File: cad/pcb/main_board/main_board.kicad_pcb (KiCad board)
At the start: 2 copper layers, 69.8 x 55.5 mm, 76 parts, among them J1 USB_B_Micro, J2 Conn_ARM_JTAG_SWD_10, U1 STM32F401R_B-C_Tx, U2 TLV75533PDRVR, Y1 Crystal_GND23

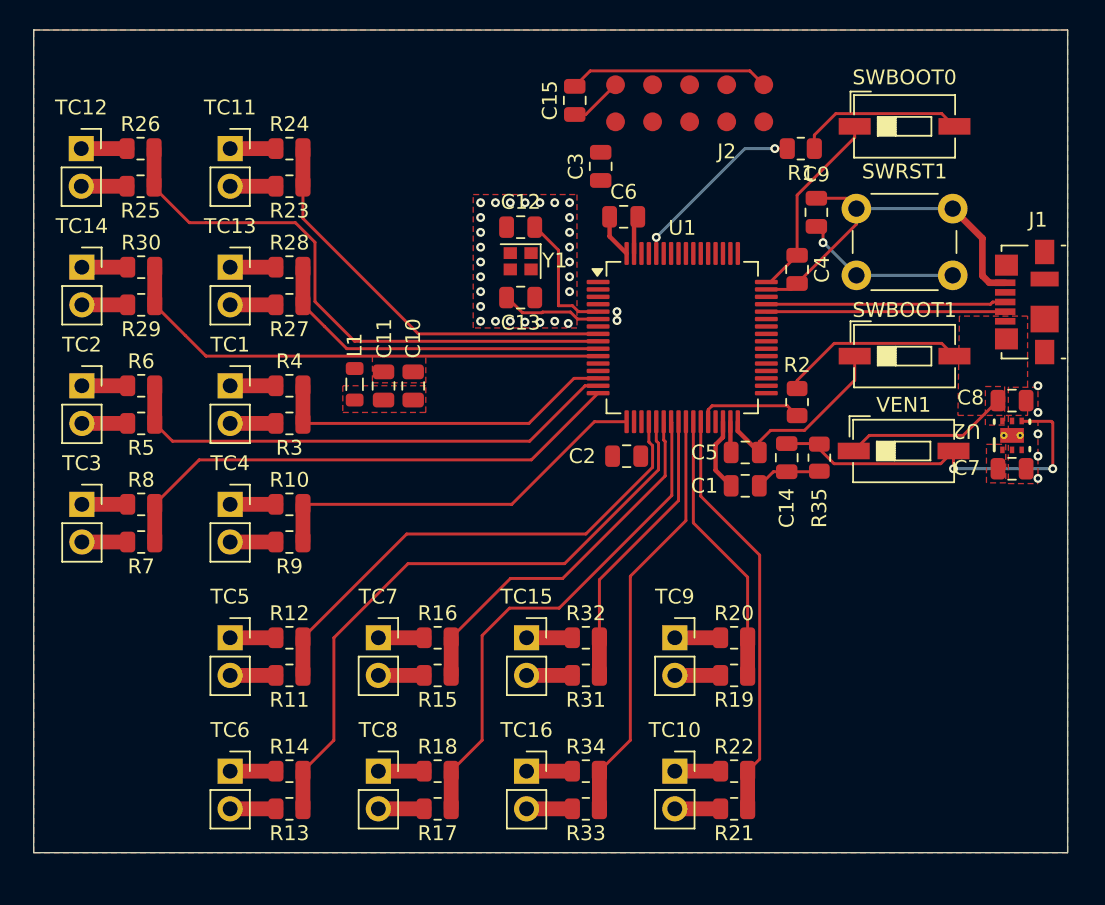
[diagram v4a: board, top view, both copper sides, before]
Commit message: Connecting NRST, placing VSS Vias next to MCU Pins
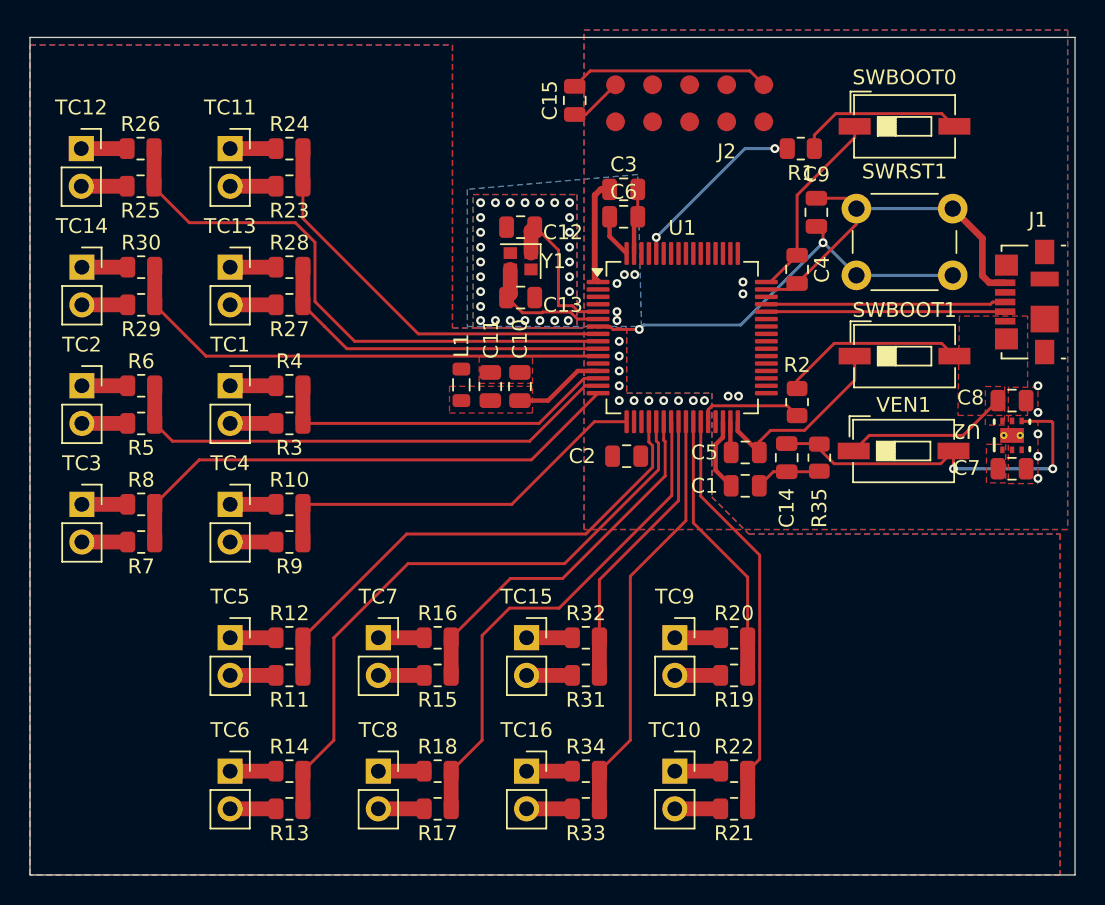
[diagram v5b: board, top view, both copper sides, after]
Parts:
- moved C10 7.20 mm to (98.5, 56.0)
- moved C11 7.20 mm to (96.5, 56.0)
- moved L1 7.20 mm to (94.6, 55.9)
- moved C3 2.19 mm to (105.5, 42.8), turned to 0 degrees
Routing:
- net Net-(U1-NRST): track 10.9 -> 28.6 mm, vias 1 -> 2
- net VDD: track 32.9 -> 40.0 mm
- net VDDA: track 0.00 -> 6.10 mm
- net Net-(U1-PH1): track 6.84 -> 8.84 mm
- net Net-(U1-PH0): track 9.21 -> 11.1 mm
- net VSS: track 35.5 -> 37.4 mm, vias 34 -> 41
- net VSSA: vias 0 -> 11
- added copper zone on B.Cu, net VSSA
- added copper zone on F.Cu, net VSSA
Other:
- board size 69.8 x 55.5 mm -> 70.5 x 56.5 mm

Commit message: Power SUpply Struggles
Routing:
- net VDD: track 40.0 -> 72.9 mm, vias 0 -> 1
- net Net-(R2-Pad1): track 12.6 -> 2.12 mm, vias 0 -> 1
- net VBUS: track 11.1 -> 1.48 mm
- net VSS: track 37.4 -> 40.3 mm
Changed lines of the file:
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@@
+	)
+	(segment
+		(start 106.25 59.30312)
+		(end 104.80312 60.75)
+		(width 0.3)
+		(layer "F.Cu")
+		(net 2)
+	)
+	(segment
+		(start 104.80312 60.75)
+		(end 104.8 60.75)
+		(width 0.3)
+		(layer "F.Cu")
+		(net 2)
+	)
+	(segment
+		(start 106.25 58.425)
+		(end 106.25 59.30312)
+		(width 0.3)
+		(layer "F.Cu")
+		(net 2)
 	)
 	(segment
@@
 	)
 	(segment
-		(start 117.75 59.009744)
-		(end 115.465256 59.009744)
-		(width 0.2)
-		(layer "F.Cu")
-		(net 3)
-	)
-	(segment
 		(start 104 42.75)
 		(end 104.6 42.75)
@@
 	)
 	(segment
+		(start 104.6 42.75)
+		(end 104.6 44.6)
+		(width 0.4)
+		(layer "F.Cu")
+		(net 3)
+	)
+	(segment
 		(start 117.25 47.2)
 		(end 115.45 49)
@@
 	)
 	(segment
+		(start 130.8 61.6)
+		(end 129.58 60.38)
+		(width 1)
+		(layer "F.Cu")
+		(net 3)
+	)
+	(segment
+		(start 106.75 58.425)
+		(end 106.75 60.7)
+		(width 0.3)
+		(layer "F.Cu")
+		(net 3)
+	)
+	(segment
+		(start 114.7 59.775)
+		(end 115.465256 59.009744)
+		(width 0.4)
+		(layer "F.Cu")
+		(net 3)
+	)
+	(segment
 		(start 103.6 43.15)
 		(end 104 42.75)
@@
 	)
 	(segment
+		(start 121.135 55.765)
+		(end 121.135 54)
+		(width 0.4)
+		(layer "F.Cu")
+		(net 3)
+	)
+	(segment
 		(start 121.135 38.5)
 		(end 121.135 39.255256)
@@
 	)
 	(segment
-		(start 121.135 55.624744)
-		(end 121.135 54)
-		(width 0.2)
+		(start 114.7 60.5)
+		(end 114.7 59.775)
+		(width 0.4)
 		(layer "F.Cu")
 		(net 3)
@@
 	)
 	(segment
-		(start 117.75 59.009744)
-		(end 121.135 55.624744)
-		(width 0.2)
+		(start 111.675 41.625)
+		(end 117.25 47.2)
+		(width 0.4)
 		(layer "F.Cu")
 		(net 3)
@@
 	)
 	(segment
+		(start 117.890256 59.009744)
+		(end 121.135 55.765)
+		(width 0.4)
+		(layer "F.Cu")
+		(net 3)
+	)
+	(segment
+		(start 105.725 41.625)
+		(end 111.675 41.625)
+		(width 0.4)
+		(layer "F.Cu")
+		(net 3)
+	)
+	(segment
+		(start 105.725 41.625)
+		(end 105.725 41.175)
+		(width 0.4)
+		(layer "F.Cu")
+		(net 3)
+	)
+	(segment
+		(start 104.6 42.75)
+		(end 105.725 41.625)
+		(width 0.4)
+		(layer "F.Cu")
+		(net 3)
+	)
+	(segment
 		(start 104.6 45.925)
 		(end 105.75 47.075)
@@
 	)
 	(segment
-		(start 115.465256 59.009744)
-		(end 114.7 59.775)
-		(width 0.2)
+		(start 129.58 60.38)
+		(end 129.58 59.3)
+		(width 1)
+		(layer "F.Cu")
+		(net 3)
+	)
+	(segment
+		(start 105.725 41.175)
+		(end 102.25 37.7)
+		(width 0.4)
+		(layer "F.Cu")
+		(net 3)
+	)
+	(segment
+		(start 129.58 59.3)
+		(end 126.045 55.765)
+		(width 1)
 		(layer "F.Cu")
 		(net 3)
@@
 	)
 	(segment
-		(start 114.7 59.775)
-		(end 114.7 60.5)
-		(width 0.2)
-		(layer "F.Cu")
-		(net 3)
-	)
-	(segment
-		(start 128.45 59.35)
-		(end 130.8 57)
-		(width 0.2)
-		(layer "F.Cu")
-		(net 4)
-	)
-	(segment
-		(start 122.12 59.35)
-		(end 128.45 59.35)
-		(width 0.2)
-		(layer "F.Cu")
-		(net 4)
+		(start 106.75 60.7)
+		(end 106.7 60.75)
+		(width 0.3)
+		(layer "F.Cu")
+		(net 3)
+	)
+	(segment
+		(start 115.465256 59.009744)
+		(end 117.890256 59.009744)
+		(width 0.4)
+		(layer "F.Cu")
+		(net 3)
+	)
+	(via
+		(at 126.045 55.765)
+		(size 0.6)
+		(drill 0.3)
+		(layers "F.Cu" "B.Cu")
+		(net 3)
 	)
 	(segment
@@
 	)
 	(segment
-		(start 117.25 55.645)
-		(end 119.755 53.14)
-		(width 0.2)
-		(layer "F.Cu")
-		(net 16)
-	)
-	(segment
 		(start 117.25 56.1875)
 		(end 117.25 55.645)
@@
 	)
 	(segment
-		(start 119.755 53.14)
-		(end 127.005 53.14)
+		(start 117.25 55.645)
+		(end 117.25 55.35)
+		(width 0.2)
+		(layer "F.Cu")
+		(net 16)
+	)
+	(segment
+		(start 117.25 55.35)
+		(end 117.2 55.3)
 		(width 0.2)
 		(layer "F.Cu")
@@
 		(net 16)
 	)
+	(via
+		(at 117.2 55.3)
+		(size 0.6)
+		(drill 0.3)
+		(layers "F.Cu" "B.Cu")
+		(net 16)
+	)

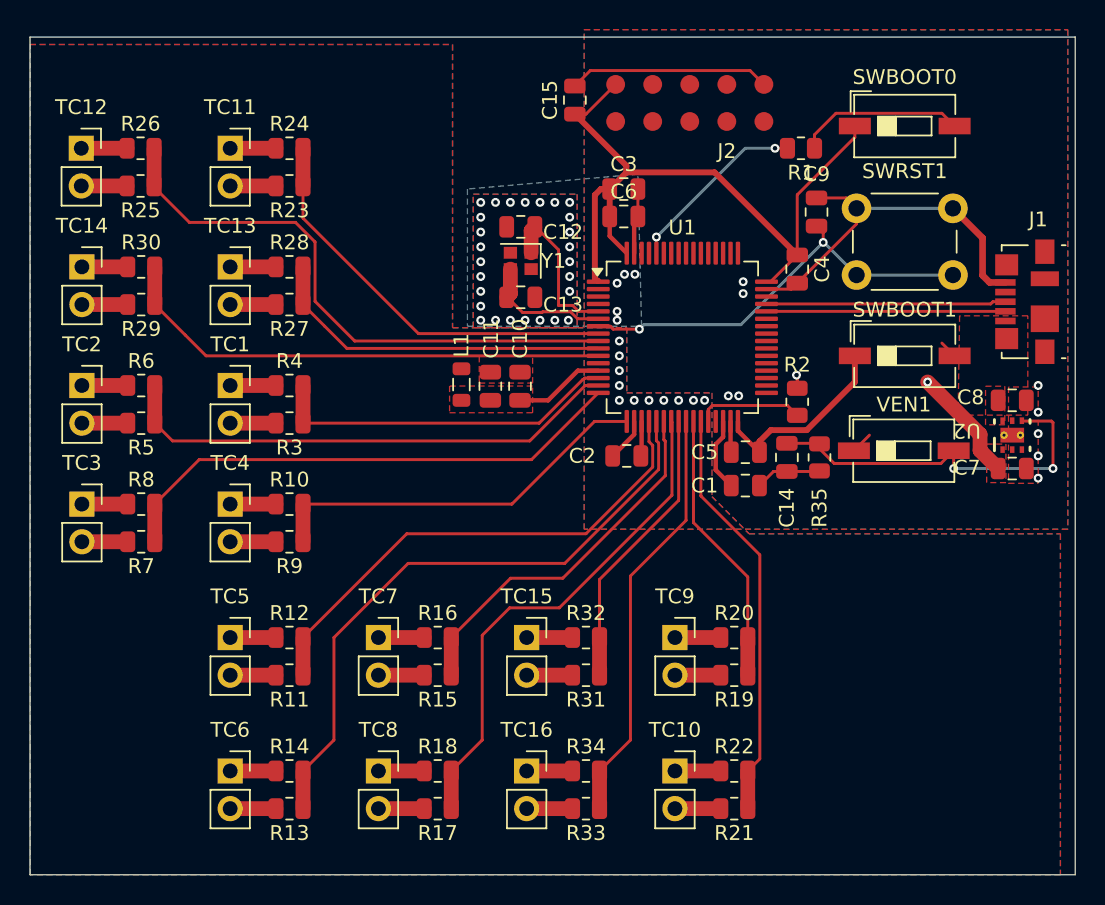
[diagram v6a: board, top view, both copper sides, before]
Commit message: DRC mostly checks out now
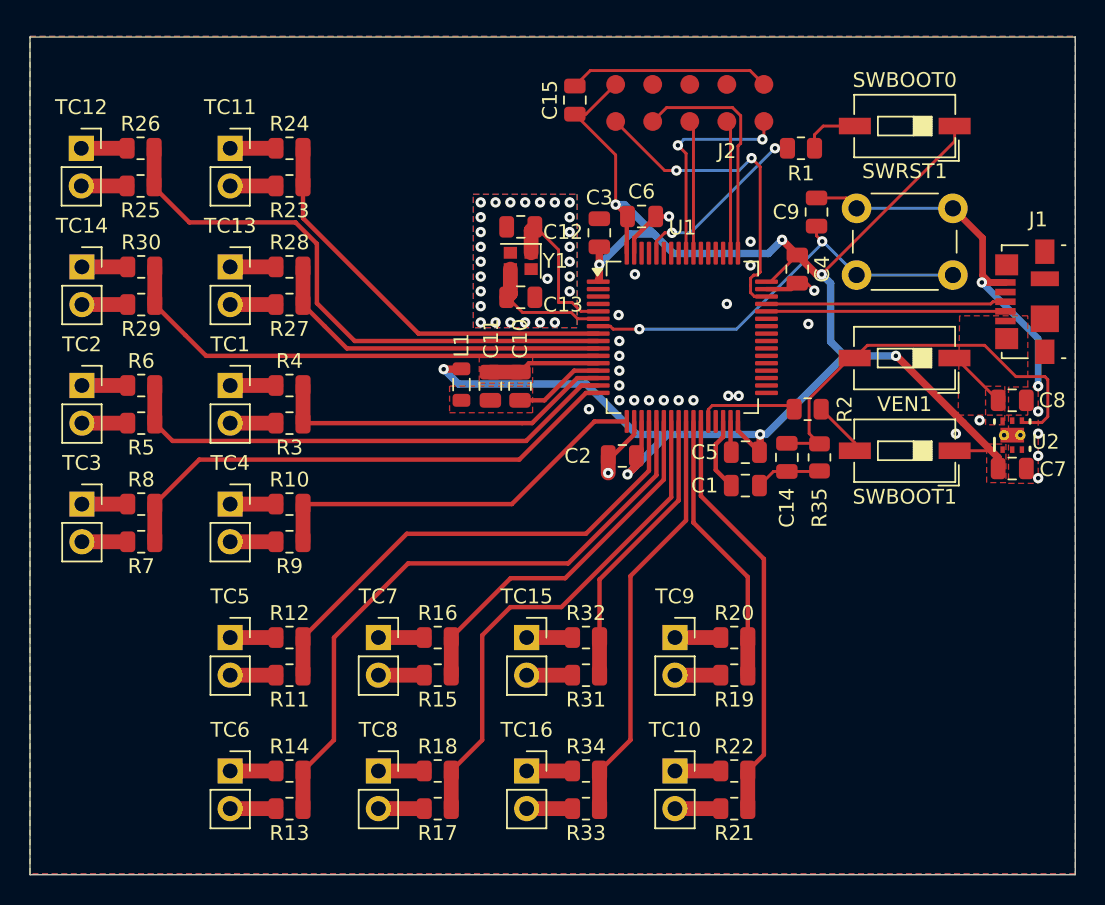
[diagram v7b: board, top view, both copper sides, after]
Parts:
- moved SWBOOT1 6.40 mm to (124.5, 60.4), turned to 180 degrees
- moved VEN1 6.25 mm to (124.5, 54.1), turned to 180 degrees
- moved C3 3.38 mm to (103.9, 45.7), turned to 90 degrees
- moved C6 1.20 mm to (106.8, 44.6)
- moved R2 0.86 mm to (118.0, 57.6), turned to 180 degrees
- moved C2 0.30 mm to (105.5, 60.8)
- turned SWBOOT0 to 180 degrees
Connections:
- R11 pad 2: VSSA -> VSS
- R13 pad 2: VSSA -> VSS
- R15 pad 2: VSSA -> VSS
- R17 pad 2: VSSA -> VSS
- R19 pad 2: VSSA -> VSS
- R21 pad 2: VSSA -> VSS
- R23 pad 2: VSSA -> VSS
- R25 pad 2: VSSA -> VSS
- R27 pad 2: VSSA -> VSS
- R29 pad 2: VSSA -> VSS
- R3 pad 2: VSSA -> VSS
- R31 pad 2: VSSA -> VSS
- R33 pad 2: VSSA -> VSS
- R5 pad 2: VSSA -> VSS
- R7 pad 2: VSSA -> VSS
- R9 pad 2: VSSA -> VSS
- TC1 pad 2: VSSA -> VSS
- TC10 pad 2: VSSA -> VSS
- TC11 pad 2: VSSA -> VSS
- TC12 pad 2: VSSA -> VSS
- TC13 pad 2: VSSA -> VSS
- TC14 pad 2: VSSA -> VSS
- TC15 pad 2: VSSA -> VSS
- TC16 pad 2: VSSA -> VSS
- TC2 pad 2: VSSA -> VSS
- TC3 pad 2: VSSA -> VSS
- TC4 pad 2: VSSA -> VSS
- TC5 pad 2: VSSA -> VSS
- TC6 pad 2: VSSA -> VSS
- TC7 pad 2: VSSA -> VSS
- TC8 pad 2: VSSA -> VSS
- TC9 pad 2: VSSA -> VSS
- U1 pad 12: VSSA -> VSS
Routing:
- net VSS: track 40.3 -> 103.8 mm, vias 41 -> 57
- net VSSA: track 49.4 -> 0.00 mm, vias 11 -> 0
- net VDD: track 72.9 -> 121.8 mm, vias 1 -> 8
- net Net-(J2-SWDIO/TMS): track 0.00 -> 21.7 mm, vias 0 -> 2
- net Net-(J2-SWCLK/TCK): track 0.00 -> 15.9 mm
- net Net-(J2-~{RESET}): track 0.00 -> 14.6 mm, vias 0 -> 2
- net Net-(J2-SWO/TDO): track 0.00 -> 8.99 mm
- net Net-(J2-NC/TDI): track 0.00 -> 8.99 mm
- net Net-(R1-Pad1): track 11.3 -> 4.15 mm
- net Net-(U2-EN): track 25.5 -> 28.9 mm, vias 2 -> 0
- net VBUS: track 1.48 -> 4.13 mm
- net Net-(R2-Pad1): track 2.12 -> 3.74 mm, vias 1 -> 0
- removed copper zone on B.Cu, net VSSA
- removed copper zone on F.Cu, net VSSA

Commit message: little wire shoving
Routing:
- net /MCU/ADC_IN11: track 39.2 -> 36.8 mm
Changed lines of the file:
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@@
 	)
 	(segment
-		(start 76.25 45)
-		(end 73.86875 42.61875)
+		(start 76.32875 45)
+		(end 73.86875 42.54)
 		(width 0.3)
 		(layer "F.Cu")
@@
 	)
 	(segment
-		(start 84.85 46.444606)
-		(end 83.405394 45)
+		(start 103.825 53)
+		(end 90.5 53)
 		(width 0.3)
 		(layer "F.Cu")
@@
 	)
 	(segment
-		(start 83.405394 45)
-		(end 76.25 45)
+		(start 90.5 53)
+		(end 82.5 45)
 		(width 0.3)
 		(layer "F.Cu")
@@
 	)
 	(segment
-		(start 73.86875 42.61875)
-		(end 73.86875 42.54)
+		(start 82.5 45)
+		(end 76.32875 45)
 		(width 0.3)
 		(layer "F.Cu")
-		(net 40)
-	)
-	(segment
-		(start 84.85 50.45)
-		(end 84.85 46.444606)
-		(width 0.3)
-		(layer "F.Cu")
-		(net 40)
-	)
-	(segment
-		(start 87.4 53)
-		(end 84.85 50.45)
-		(width 0.3)
-		(layer "F.Cu")
-		(net 40)
-	)
-	(segment
-		(start 103.825 53)
-		(end 87.4 53)
-		(width 0.3)
-		(layer "F.Cu")
